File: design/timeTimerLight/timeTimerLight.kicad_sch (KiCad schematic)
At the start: 2 parts, among them Q1 2N3906, U1 MCP1640x-xCHY

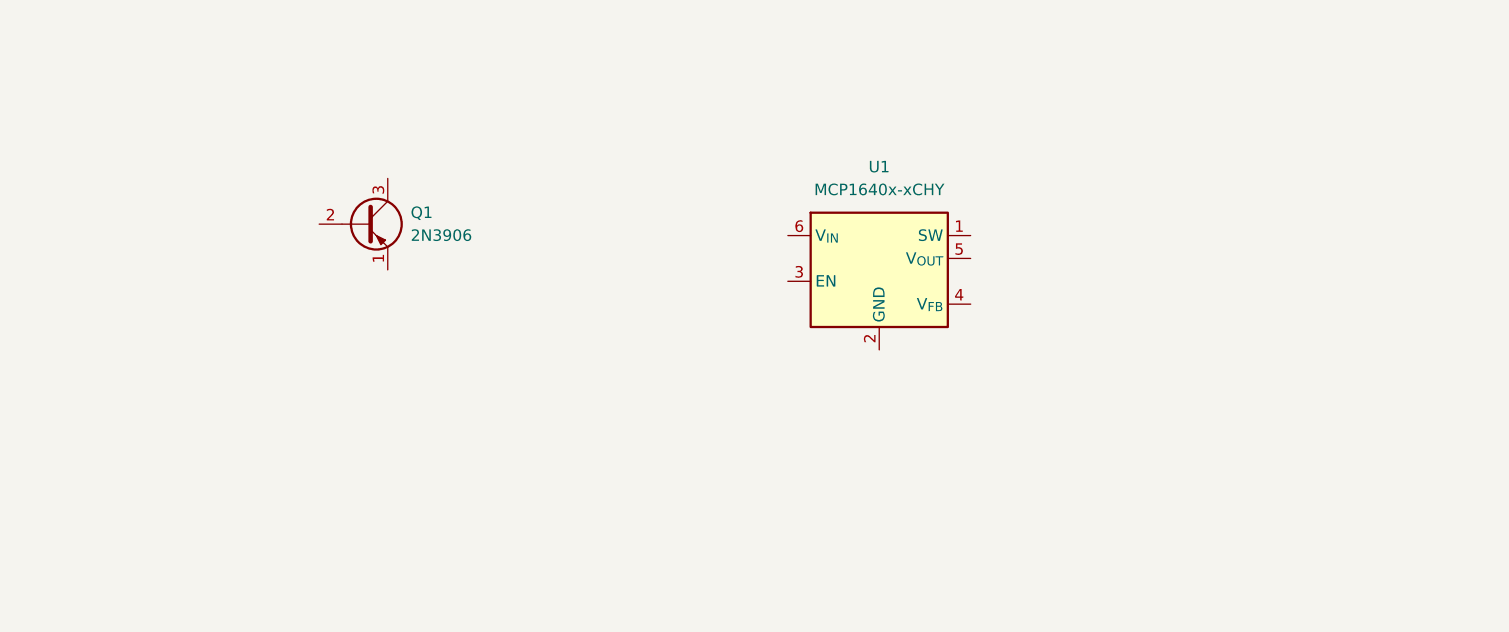
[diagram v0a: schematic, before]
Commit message: Schematic for time timer done.
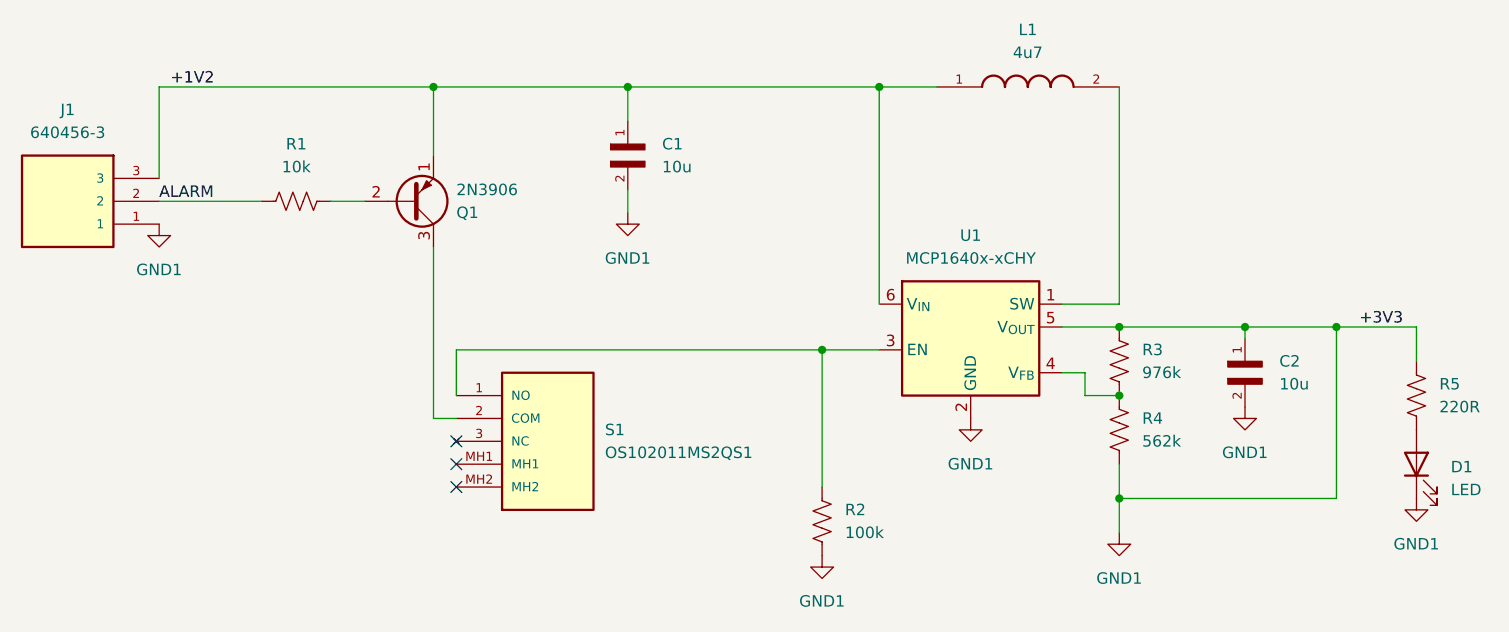
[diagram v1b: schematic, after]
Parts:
- added C1, C2: 10u, customParts:CAPRB250W50L400T250H550, symbol FK18X5R0J106MR020:FK18X5R0J106MR020
- added D1: LED, LED_THT:LED_D5.0mm, symbol Device:LED
- added J1: 640456-3, customParts:TE_640456-3, symbol 640456-3:640456-3
- added L1: 4u7, customParts:IND_CDRH2D18_HPNP-4R7NC, symbol CDRH2D18_HPNP-4R7NC:CDRH2D18_HPNP-4R7NC
- added R1: 10k, customParts:RESAD1100W55L630D240B, symbol Device:R_US
- added R2: 100k, customParts:RESAD1100W55L630D240B, symbol Device:R_US
- added R3: 976k, customParts:RESAD1100W55L630D240B, symbol Device:R_US
- added R4: 562k, customParts:RESAD1100W55L630D240B, symbol Device:R_US
- added R5: 220R, customParts:RESAD1100W55L630D240B, symbol Device:R_US
- added S1: OS102011MS2QS1, customParts:OS102011MS2QS1, symbol OS102011MS2QS1:OS102011MS2QS1
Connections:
- net at U1.1 (SW): now also L1.2
- net GND1: now reaches U1.2 (GND)
- net GND1: now also U1.5 (V_{OUT}), C1.2, C2.1, C2.2, D1.1 (K), J1.1, R2.2, R3.1, R4.2, R5.1
- net at U1.3 (EN): now also R2.1, S1.1 (NO)
- net at U1.4 (V_{FB}): now also R3.2, R4.1
- net +1V2: now reaches U1.6 (V_{IN})
- net +1V2: now also Q1.1 (E), C1.1, J1.3, L1.1
- net at Q1.2 (B): now also R1.1
- net at Q1.3 (C): now also S1.2 (COM)
- new net: D1.2 (A), R5.2
- new net ALARM: J1.2, R1.2
- no-connect marks 0 -> 3
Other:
- moved on the sheet: Q1, U1

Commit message: Got components layed out on PCB editor, no traces yet.  Switched to right-angle connector.
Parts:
- removed J1: 640456-3, customParts:TE_640456-3, symbol 640456-3:640456-3
- added J1: 640455-3, customParts:TE_640455-3, symbol 640455-3:640455-3
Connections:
- net +1V2: now also J1.3
- net ALARM: now also J1.2
- net GND1: now also J1.1
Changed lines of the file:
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@@
+	)
+	(symbol
+		(lib_id "640455-3:640455-3")
+		(at 46.99 77.47 180)
+		(unit 1)
+		(exclude_from_sim no)
+		(in_bom yes)
+		(on_board yes)
+		(dnp no)
+		(fields_autoplaced yes)
+		(property "Reference" "J1"
+			(at 46.99 67.31 0)
+			(effects
+				(font
+					(size 1.27 1.27)
+				)
+			)
+		)
+		(property "Value" "640455-3"
+			(at 46.99 69.85 0)
+			(effects
+				(font
+					(size 1.27 1.27)
+				)
+			)
+		)
+		(property "Footprint" "customParts:TE_640455-3"
+			(at 46.99 77.47 0)
+			(effects
+				(font
+					(size 1.27 1.27)
+				)
+				(justify bottom)
+				(hide yes)
+			)
+		)
+		(property "Datasheet" ""
+			(at 46.99 77.47 0)
+			(effects
+				(font
+					(size 1.27 1.27)
+				)
+				(hide yes)
+			)
+		)
+		(property "Description" ""
+			(at 46.99 77.47 0)
+			(effects
+				(font
+					(size 1.27 1.27)
+				)
+				(hide yes)
+			)
+		)
+		(property "PARTREV" "R"
+			(at 46.99 77.47 0)
+			(effects
+				(font
+					(size 1.27 1.27)
+				)
+				(justify bottom)
+				(hide yes)
+			)
+		)
+		(property "STANDARD" "Manufacturer Recommendations"
+			(at 46.99 77.47 0)
+			(effects
+				(font
+					(size 1.27 1.27)
+				)
+				(justify bottom)
+				(hide yes)
+			)
+		)
+		(property "MANUFACTURER" "TE"
+			(at 46.99 77.47 0)
+			(effects
+				(font
+					(size 1.27 1.27)
+				)
+				(justify bottom)
+				(hide yes)
+			)
+		)
+		(pin "3"
+		)
+		(pin "1"
+		)
+		(pin "2"
+		)
+		(instances
+			(project ""
+				(path "/a9e9f5c2-aacb-4f9c-896b-ad3263a34d8b"
+					(reference "J1")
+					(unit 1)
+				)
+			)
+		)
 	)
 	(symbol
@@
 					(unit 1)
 				)
-			)
-		)
-	)
-	(symbol
-		(lib_id "640456-3:640456-3")
-		(at 46.99 77.47 180)
-		(unit 1)
-		(exclude_from_sim no)
-		(in_bom yes)
-		(on_board yes)
-		(dnp no)
-		(fields_autoplaced yes)
-		(property "Reference" "J1"
-			(at 46.99 67.31 0)
-			(effects
-				(font
-					(size 1.27 1.27)
-				)
-			)
-		)
-		(property "Value" "640456-3"
-			(at 46.99 69.85 0)
-			(effects
-				(font
-					(size 1.27 1.27)
-				)
-			)
-		)
-		(property "Footprint" "customParts:TE_640456-3"
-			(at 46.99 77.47 0)
-			(effects
-				(font
-					(size 1.27 1.27)
-				)
-				(justify bottom)
-				(hide yes)
-			)
-		)
-		(property "Datasheet" ""
-			(at 46.99 77.47 0)
-			(effects
-				(font
-					(size 1.27 1.27)
-				)
-				(hide yes)
-			)
-		)
-		(property "Description" ""
-			(at 46.99 77.47 0)
-			(effects
-				(font
-					(size 1.27 1.27)
-				)
-				(hide yes)
-			)
-		)
-		(property "PARTREV" "R"
-			(at 46.99 77.47 0)
-			(effects
-				(font
-					(size 1.27 1.27)
-				)
-				(justify bottom)
-				(hide yes)
-			)
-		)
-		(property "STANDARD" "Manufacturer Recommendations"
-			(at 46.99 77.47 0)
-			(effects
-				(font
-					(size 1.27 1.27)
-				)
-				(justify bottom)
-				(hide yes)
-			)
-		)
-		(property "MANUFACTURER" "TE"
-			(at 46.99 77.47 0)
-			(effects
-				(font
-					(size 1.27 1.27)
-				)
-				(justify bottom)
-				(hide yes)
-			)
-		)
-		(pin "3"
-		)
-		(pin "2"
-		)
-		(pin "1"
-		)
-		(instances
-			(project ""
-				(path "/a9e9f5c2-aacb-4f9c-896b-ad3263a34d8b"
-					(reference "J1")
-					(unit 1)
-				)

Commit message: Fixed some traces.  Moved part descriptions to main silk layer.
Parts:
- U1: value MCP1640x-xCHY -> MCP1640T-I/CHY
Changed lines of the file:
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@@
 			)
 		)
-		(property "Value" "MCP1640x-xCHY"
+		(property "Value" "MCP1640T-I/CHY"
 			(at 147.32 83.82 0)
 			(effects

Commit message: Whoops, original schematic had a short circuit to ground on Vout 3.3v.  Breadboard prototype did not have this, but fixed it in schematic and PCB... Close call!
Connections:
- net GND1: no longer C2.1, R3.1, R5.1, U1.5 (V_{OUT})
- new net +3V3: C2.1, R3.1, R5.1, U1.5 (V_{OUT})
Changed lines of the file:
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@@
-	)
-	(junction
-		(at 187.96 91.44)
-		(diameter 0)
-		(color 0 0 0 0)
-	)
-	(junction
-		(at 163.83 110.49)
-		(diameter 0)
-		(color 0 0 0 0)
 	)
 	(junction
@@
 	(wire
 		(pts
-			(xy 177.8 91.44) (xy 187.96 91.44)
+			(xy 177.8 91.44) (xy 196.85 91.44)
 		)
 		(stroke
@@
 	(wire
 		(pts
-			(xy 163.83 110.49) (xy 163.83 106.68)
-		)
-		(stroke
-			(width 0)
-			(type default)
-		)
-	)
-	(wire
-		(pts
 			(xy 196.85 91.44) (xy 196.85 95.25)
 		)
@@
 	(wire
 		(pts
-			(xy 187.96 91.44) (xy 196.85 91.44)
-		)
-		(stroke
-			(width 0)
-			(type default)
-		)
-	)
-	(wire
-		(pts
 			(xy 109.22 64.77) (xy 137.16 64.77)
 		)
@@
 	(wire
 		(pts
-			(xy 163.83 110.49) (xy 187.96 110.49)
-		)
-		(stroke
-			(width 0)
-			(type default)
-		)
-	)
-	(wire
-		(pts
 			(xy 87.63 101.6) (xy 90.17 101.6)
 		)
@@
 	(wire
 		(pts
-			(xy 187.96 91.44) (xy 187.96 110.49)
-		)
-		(stroke
-			(width 0)
-			(type default)
-		)
-	)
-	(wire
-		(pts
 			(xy 90.17 93.98) (xy 130.81 93.98)
 		)
@@
 	(wire
 		(pts
-			(xy 163.83 114.3) (xy 163.83 110.49)
-		)
-		(stroke
+			(xy 163.83 106.68) (xy 163.83 114.3)
+		)
+		(stroke
